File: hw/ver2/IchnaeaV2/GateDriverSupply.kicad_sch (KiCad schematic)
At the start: 0 parts

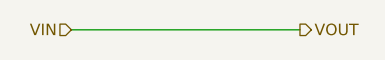
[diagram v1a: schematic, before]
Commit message: Not quite happy with the power stage just yet.
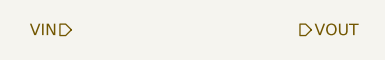
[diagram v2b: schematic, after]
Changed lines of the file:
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@@
 	(generator_version "8.0")
 	(paper "A4")
-	(wire
-		(pts
-			(xy 100.33 78.74) (xy 125.73 78.74)
-		)
-		(stroke
-			(width 0)
-			(type default)
-		)
-	)
 	(hierarchical_label "VIN"
 		(shape input)

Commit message: Sync work to main PC
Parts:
- added C74, C78, C79, C80, C81: 10uF, Capacitor_SMD:C_0603_1608Metric, symbol Device:C
- added C75: 4.7uF, Capacitor_SMD:C_0603_1608Metric, symbol Device:C
- added C76, C82: 100nF, Capacitor_SMD:C_0603_1608Metric, symbol Device:C
- added C77: 47pF, Capacitor_SMD:C_0603_1608Metric, symbol Device:C
- added D10: SS210, Diode_SMD:D_SMA, symbol Device:D_Schottky
- added L7: 22uH, Inductors:TYS5020220M, symbol Device:L_Ferrite
- added R57: 68k, Resistor_SMD:R_0603_1608Metric, symbol Device:R_US
- added R58: 510k, Resistor_SMD:R_0603_1608Metric, symbol Device:R_US
- added R59: 7.5k, Resistor_SMD:R_0603_1608Metric, symbol Device:R_US
- added R60: 100k, Resistor_SMD:R_0603_1608Metric, symbol Device:R_US
- added U8: AP66200FVBW-13, Package_DFN_QFN:QFN-16-1EP_4x4mm_P0.65mm_EP2.5x2.5mm, symbol ap66200:AP66200FVBW
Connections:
- net VIN: now also D10.2 (A)
- net VOUT: now also C77.2, C78.1, C79.1, C80.1, C81.1, C82.1, L7.2, R60.2
- new net: C74.1, D10.1 (K), R57.1, R58.1, U8.3 (VIN), U8.4 (VIN)
- new net: C76.1, U8.5 (BOOST)
- new net: C76.2, L7.1, U8.6 (SW), U8.7 (SW)
- new net: C77.1, R59.1, R60.1, U8.15 (FB)
- new net: R58.2, U8.10 (EN)
- new net AP_VCC: C75.1, U8.11 (FS), U8.14 (SS), U8.2 (VCC)
- new net GND: C74.2, C75.2, C78.2, C79.2, C80.2, C81.2, C82.2, R57.2, R59.2, U8.12 (MSYNC), U8.16 (GND), U8.17 (EPAD), U8.8 (PGND), U8.9 (PGND)
- new net VOUT_LV: U8.1 (BIAS)
- no-connect marks 0 -> 1
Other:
- note added: "1. Update voltage references 2. Update UVLO 3. Update schematic for part number 4. Potentially make voltage reference selectable?"
- note added: "Fig.40, sets UVLO ~12v."
